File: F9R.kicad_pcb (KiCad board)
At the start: 4 copper layers, 90 x 50 mm, 73 parts, among them J1 JST_GH, J2 Molex_PicoBlade, J3 CONN_06NO_SILK_FEMALE_PTH, J4 Conn_01x06, P1 USB_C_Plug_USB2.0, U1 ZED-F9R, U2 DUAL-OPTO_HCPL-073L, U3 LD1117S33TR, U4 UHS_INVERTER_SCHMITT_TRIGGERS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, U5 UHS_INVERTER_SCHMITT_TRIGGERS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

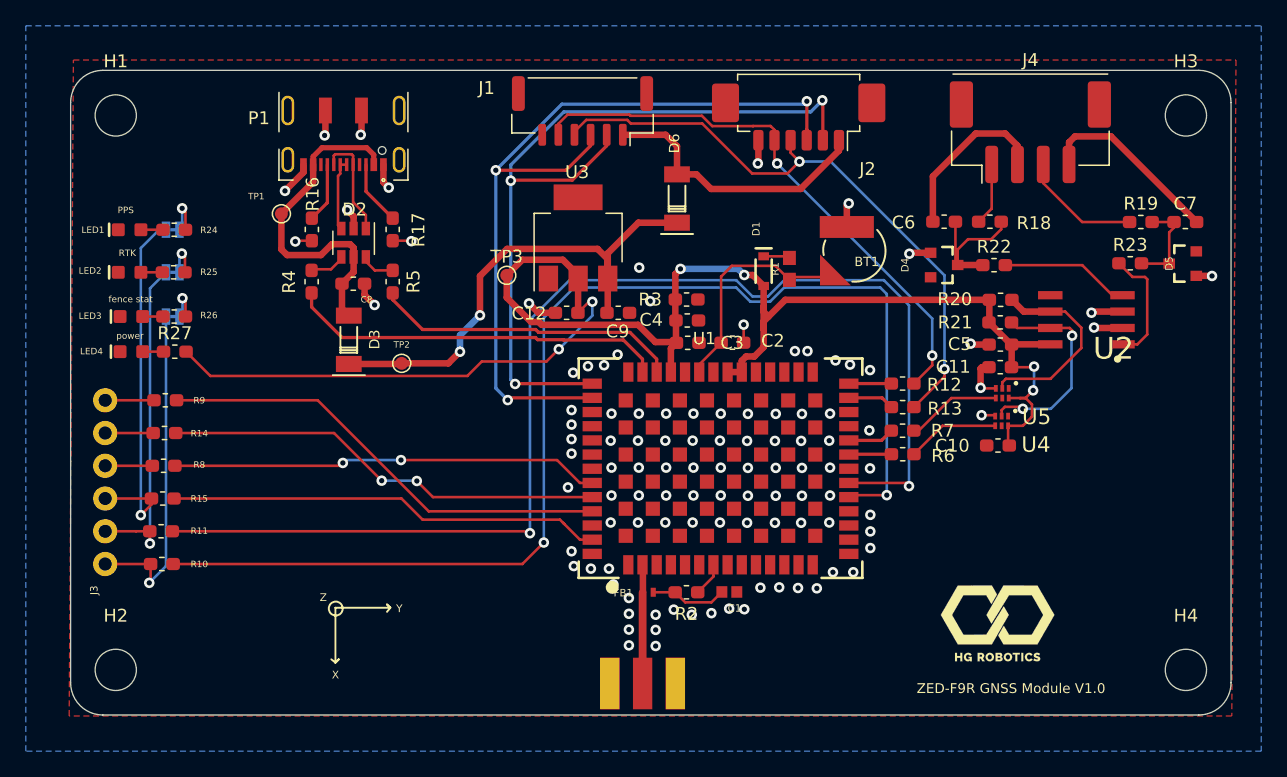
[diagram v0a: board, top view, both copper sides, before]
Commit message: edited silk screen
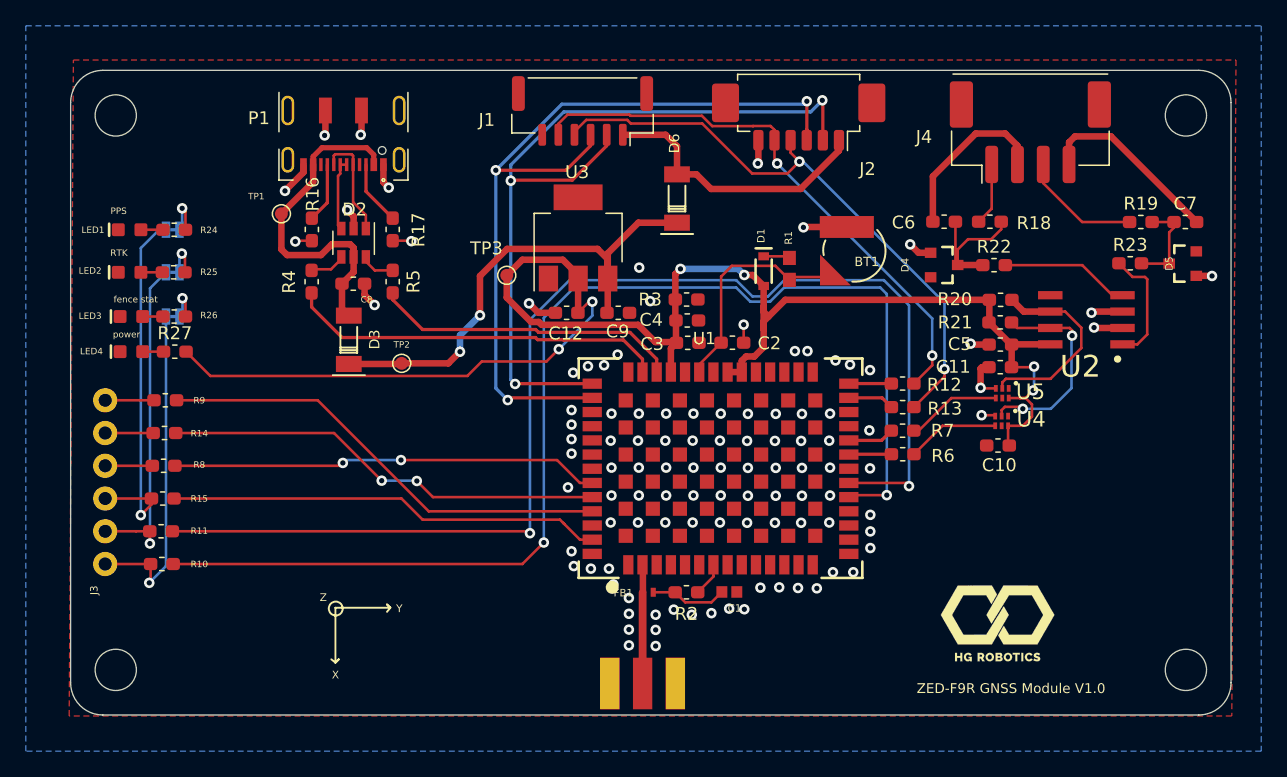
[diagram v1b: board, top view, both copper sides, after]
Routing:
- net GND: track 63.7 -> 65.3 mm
- net /RX2: track 48.2 -> 47.0 mm
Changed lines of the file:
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@@
   )
   (setup
-    (last_trace_width 0.2032)
+    (last_trace_width 0.508)
     (user_trace_width 0.254)
     (user_trace_width 0.3048)
@@
     (tags "connector Molex CLIK-Mate side entry")
     (attr smd)
-    (fp_text reference J4 (at 0 -5.6) (layer F.SilkS)
+    (fp_text reference J4 (at -8.255 0.3683) (layer F.SilkS)
       (effects (font (size 1 1) (thickness 0.15)))
     )
@@
     (at 192.25 75.05 180)
     (descr "<h3>SIP6 Package</h3>\n<ul>\n<li>Total Size: 1.45mm x 1mm</li>\n<li>Pad Size: .3mm x .52mm</li>\n<li>Pitch: .5mm</li>\n<li></li>\n<li></li>\n<li></li>\n</ul>")
-    (fp_text reference U5 (at -3.802 -2.534332) (layer F.SilkS)
+    (fp_text reference U5 (at -3.33 -0.5912) (layer F.SilkS)
       (effects (font (size 1.2065 1.2065) (thickness 0.09652)) (justify right bottom))
     )
@@
     (at 192.2 77.2 180)
     (descr "<h3>SIP6 Package</h3>\n<ul>\n<li>Total Size: 1.45mm x 1mm</li>\n<li>Pad Size: .3mm x .52mm</li>\n<li>Pitch: .5mm</li>\n<li></li>\n<li></li>\n<li></li>\n</ul>")
-    (fp_text reference U4 (at -3.802 -2.534332) (layer F.SilkS)
+    (fp_text reference U4 (at -3.4308 -0.5748) (layer F.SilkS)
       (effects (font (size 1.2065 1.2065) (thickness 0.09652)) (justify right bottom))
     )
@@
     (at 198.66 69.22 180)
     (descr "<h3>Small Outline Package 8-Pin</h3>\n\nMechanical Specifications\n<ul>\n<li>Total Size: 6mm x 5mm</li>\n<li>Body Size: 4mm x 5mm</li>\n<li>Pad Size: 1.9mm x .64mm </li>\n<li>Pad Pitch: 1.270mm</li>\n<li>8 total Pins</li>\n<li></li>\n<li></li>\n<li></li>\n<li></li>\n</ul>")
-    (fp_text reference U2 (at -3.805 -3.349332 180) (layer F.SilkS)
+    (fp_text reference U2 (at -1.238 -4.7448 180) (layer F.SilkS)
       (effects (font (size 1.6891 1.6891) (thickness 0.135128)) (justify right bottom))
     )
@@
     (tags "capacitor handsolder")
     (attr smd)
-    (fp_text reference C10 (at 3.55 -0.017) (layer F.SilkS)
+    (fp_text reference C10 (at -0.099 -1.5196) (layer F.SilkS)
       (effects (font (size 1 1) (thickness 0.15)))
     )
@@
     (at 173.75 65.575 270)
     (descr "SOD-323 (Small Outline Diode)")
-    (fp_text reference D1 (at -3.272 0.2429 90) (layer F.SilkS)
+    (fp_text reference D1 (at -2.7354 -0.1384 90) (layer F.SilkS)
       (effects (font (size 0.57912 0.57912) (thickness 0.115824)) (justify bottom))
     )
@@
     (at 175.75 65.4 90)
     (descr "<p><b>Generic 1608 (0603) package</b></p>\n<p>0.2mm courtyard excess rounded to nearest 0.05mm.</p>")
-    (fp_text reference R1 (at 0 -0.762 90) (layer F.SilkS)
+    (fp_text reference R1 (at 2.408 0.272 90) (layer F.SilkS)
       (effects (font (size 0.57912 0.57912) (thickness 0.115824)) (justify bottom))
     )
@@
     (tags "connector JST GH top entry")
     (attr smd)
-    (fp_text reference J1 (at 7.4422 1.7818) (layer F.SilkS)
+    (fp_text reference J1 (at 7.4295 -0.6985) (layer F.SilkS)
       (effects (font (size 1 1) (thickness 0.15)))
     )
@@
     (tags "capacitor handsolder")
     (attr smd)
-    (fp_text reference C3 (at 3.4474 0.0002) (layer F.SilkS)
+    (fp_text reference C3 (at -2.7608 0.0849) (layer F.SilkS)
       (effects (font (size 1 1) (thickness 0.15)))
     )
@@
     (tags "capacitor handsolder")
     (attr smd)
-    (fp_text reference C12 (at -2.92 0.05) (layer F.SilkS)
+    (fp_text reference C12 (at -0.0774 1.6024) (layer F.SilkS)
       (effects (font (size 1 1) (thickness 0.15)))
     )
@@
     (tags "capacitor handsolder")
     (attr smd)
-    (fp_text reference C2 (at 3.1372 -0.1475) (layer F.SilkS)
+    (fp_text reference C2 (at 2.8682 0.0458) (layer F.SilkS)
       (effects (font (size 1 1) (thickness 0.15)))
     )
@@
     (tags "test point SMD pad")
     (attr virtual)
-    (fp_text reference TP3 (at 0 -1.448) (layer F.SilkS)
+    (fp_text reference TP3 (at -1.5774 -2.0952) (layer F.SilkS)
       (effects (font (size 1 1) (thickness 0.15)))
     )
@@
     (tags "mounting hole 3.2mm no annular m3")
     (attr virtual)
-    (fp_text reference H4 (at 0 -4.2) (layer F.SilkS)
+    (fp_text reference H4 (at 0 -4.2) (layer F.SilkS) hide
       (effects (font (size 1 1) (thickness 0.15)))
     )
@@
     (tags "mounting hole 3.2mm no annular m3")
     (attr virtual)
-    (fp_text reference H3 (at 0 -4.2) (layer F.SilkS)
+    (fp_text reference H3 (at 0.129 3.0658) (layer F.SilkS) hide
       (effects (font (size 1 1) (thickness 0.15)))
     )
@@
     (tags "mounting hole 3.2mm no annular m3")
     (attr virtual)
-    (fp_text reference H2 (at 0 -4.2) (layer F.SilkS)
+    (fp_text reference H2 (at 0 -4.2) (layer F.SilkS) hide
       (effects (font (size 1 1) (thickness 0.15)))
     )
@@
     (tags "mounting hole 3.2mm no annular m3")
     (attr virtual)
-    (fp_text reference H1 (at 0 -4.2) (layer F.SilkS)
+    (fp_text reference H1 (at 2.5602 4.3104) (layer F.SilkS) hide
       (effects (font (size 1 1) (thickness 0.15)))
     )
-    (fp_text value MountingHole (at 0 4.2) (layer F.Fab)
+    (fp_text value MountingHole (at 0 4.2) (layer F.Fab) hide
       (effects (font (size 1 1) (thickness 0.15)))
     )
@@
   (gr_line (start 144.7927 91.6813) (end 144.5387 91.4273) (layer F.SilkS) (width 0.15))
   (gr_line (start 140.5382 91.6813) (end 144.7927 91.6813) (layer F.SilkS) (width 0.15))
-  (gr_text PPS (at 124.275 60.845) (layer F.SilkS)
+  (gr_text PPS (at 123.7234 60.9092) (layer F.SilkS)
     (effects (font (size 0.5 0.5) (thickness 0.125)))
   )
-  (gr_text power (at 124.6 70.595) (layer F.SilkS)
+  (gr_text power (at 124.333 70.485) (layer F.SilkS)
     (effects (font (size 0.5 0.5) (thickness 0.125)))
   )
-  (gr_text "RTK\n" (at 124.4 64.17) (layer F.SilkS)
+  (gr_text "RTK\n" (at 123.7488 64.1604) (layer F.SilkS)
     (effects (font (size 0.5 0.5) (thickness 0.125)))
   )
-  (gr_text "fence stat\n" (at 124.6505 67.7545) (layer F.SilkS)
+  (gr_text "fence stat\n" (at 125.0442 67.7672) (layer F.SilkS)
     (effects (font (size 0.5 0.5) (thickness 0.125)))
   )
@@
   (segment (start 208.515 65.94) (end 208.525 65.95) (width 0.508) (layer F.Cu) (net 2))
   (segment (start 208.34 65.94) (end 208.515 65.94) (width 0.508) (layer F.Cu) (net 2))
-  (via (at 180.35 60.325) (size 0.8128) (drill 0.4064) (layers F.Cu B.Cu) (net 2))
-  (segment (start 180.2 60.475) (end 180.35 60.325) (width 0.508) (layer F.Cu) (net 2))
-  (segment (start 180.2 62.15) (end 180.2 60.475) (width 0.508) (layer F.Cu) (net 2))
   (segment (start 157.5968 68.8064) (end 156.2814 68.8064) (width 0.508) (layer F.Cu) (net 2))
   (segment (start 156.2814 68.8064) (end 155.55 68.075) (width 0.508) (layer F.Cu) (net 2))
@@
   (segment (start 173.3415 57.1835) (end 173.3 57.225) (width 0.508) (layer F.Cu) (net 2))
   (segment (start 173.3415 55.4225) (end 173.3415 57.1835) (width 0.508) (layer F.Cu) (net 2))
-  (via (at 185.05 64.225) (size 0.8128) (drill 0.4064) (layers F.Cu B.Cu) (net 2))
-  (segment (start 185.125 64.15) (end 185.05 64.225) (width 0.508) (layer F.Cu) (net 2))
-  (segment (start 186.7 64.15) (end 185.125 64.15) (width 0.508) (layer F.Cu) (net 2))
   (via (at 190.575 74.625) (size 0.8128) (drill 0.4064) (layers F.Cu B.Cu) (net 2))
   (segment (start 190.619 74.669) (end 190.575 74.625) (width 0.2032) (layer F.Cu) (net 2))
@@
   (via (at 176.657 85.09) (size 0.8128) (drill 0.4064) (layers F.Cu B.Cu) (net 2))
   (via (at 172.466 85.09) (size 0.8128) (drill 0.4064) (layers F.Cu B.Cu) (net 2))
+  (segment (start 185.7652 64.15) (end 185.1152 63.5) (width 0.508) (layer F.Cu) (net 2))
+  (via (at 185.1152 63.5) (size 0.8128) (drill 0.4064) (layers F.Cu B.Cu) (net 2))
+  (segment (start 186.7 64.15) (end 185.7652 64.15) (width 0.508) (layer F.Cu) (net 2))
+  (via (at 176.8348 62.1792) (size 0.8128) (drill 0.4064) (layers F.Cu B.Cu) (net 2))
+  (segment (start 176.864 62.15) (end 176.8348 62.1792) (width 0.508) (layer F.Cu) (net 2))
+  (segment (start 180.2 62.15) (end 176.864 62.15) (width 0.508) (layer F.Cu) (net 2))
   (segment (start 165.188 90.4818) (end 166.888 90.4818) (width 0.2032) (layer F.Cu) (net 3))
   (segment (start 167.66781 91.26161) (end 169.70319 91.26161) (width 0.2032) (layer F.Cu) (net 3))
@@
   (segment (start 163.16589 53.84469) (end 163.4462 54.125) (width 0.2032) (layer F.Cu) (net 30))
   (segment (start 159.0775 54.9995) (end 159.0775 54.7563) (width 0.2032) (layer F.Cu) (net 30))
-  (segment (start 176.525 57.075) (end 178.952578 57.075) (width 0.2032) (layer B.Cu) (net 30))
-  (segment (start 178.952578 57.075) (end 187.775 65.897422) (width 0.2032) (layer B.Cu) (net 30))
-  (segment (start 187.775 65.897422) (end 187.775 73.175) (width 0.2032) (layer B.Cu) (net 30))
+  (segment (start 176.8106 57.075) (end 187.775 68.0394) (width 0.2032) (layer B.Cu) (net 30))
+  (segment (start 176.525 57.075) (end 176.8106 57.075) (width 0.2032) (layer B.Cu) (net 30))
+  (segment (start 187.775 68.0394) (end 187.775 73.175) (width 0.2032) (layer B.Cu) (net 30))
   (segment (start 122.682 75.5904) (end 126.467 75.5904) (width 0.2032) (layer F.Cu) (net 31))
   (segment (start 122.682 78.1304) (end 126.40132 78.1304) (width 0.2032) (layer F.Cu) (net 32))
